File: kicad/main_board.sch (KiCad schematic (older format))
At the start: 55 parts, among them J1 Conn_01x07, J2 Conn_01x07, J3 Conn_01x07, J4 Conn_01x07, J5 Conn_01x07, J6 TYPE-C-31-M-12, J7 TYPE-C-31-M-12, Q1 Q_NPN_BEC, Q2 Q_NPN_BEC, Q3 Q_NPN_BEC, Q4 Q_NPN_BEC, Q5 Q_NPN_BEC, SW1 Reset, SW2 Boot, U1 esp32-s2-wroom, U2 XC6220B331MR, U3 USBLC6-2SC6, U4 USBLC6-2SC6, U5 LMV324, U6 LMV324

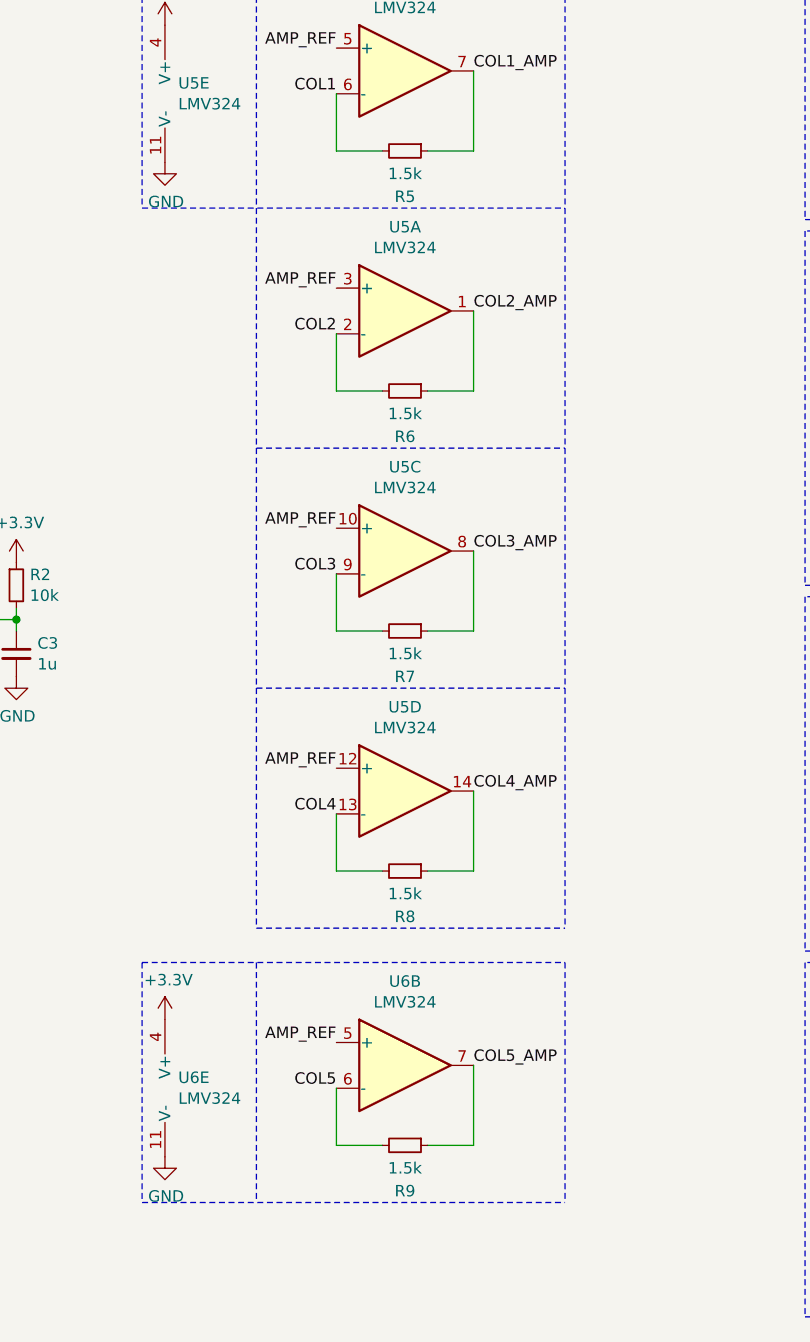
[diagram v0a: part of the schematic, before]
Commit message: Update the various sensitivity-related resistor values
This updates the transimpedance amplifier resistors to 2k, and adjusts
the LED drive resistors to an appropriate level, from empirical testing.
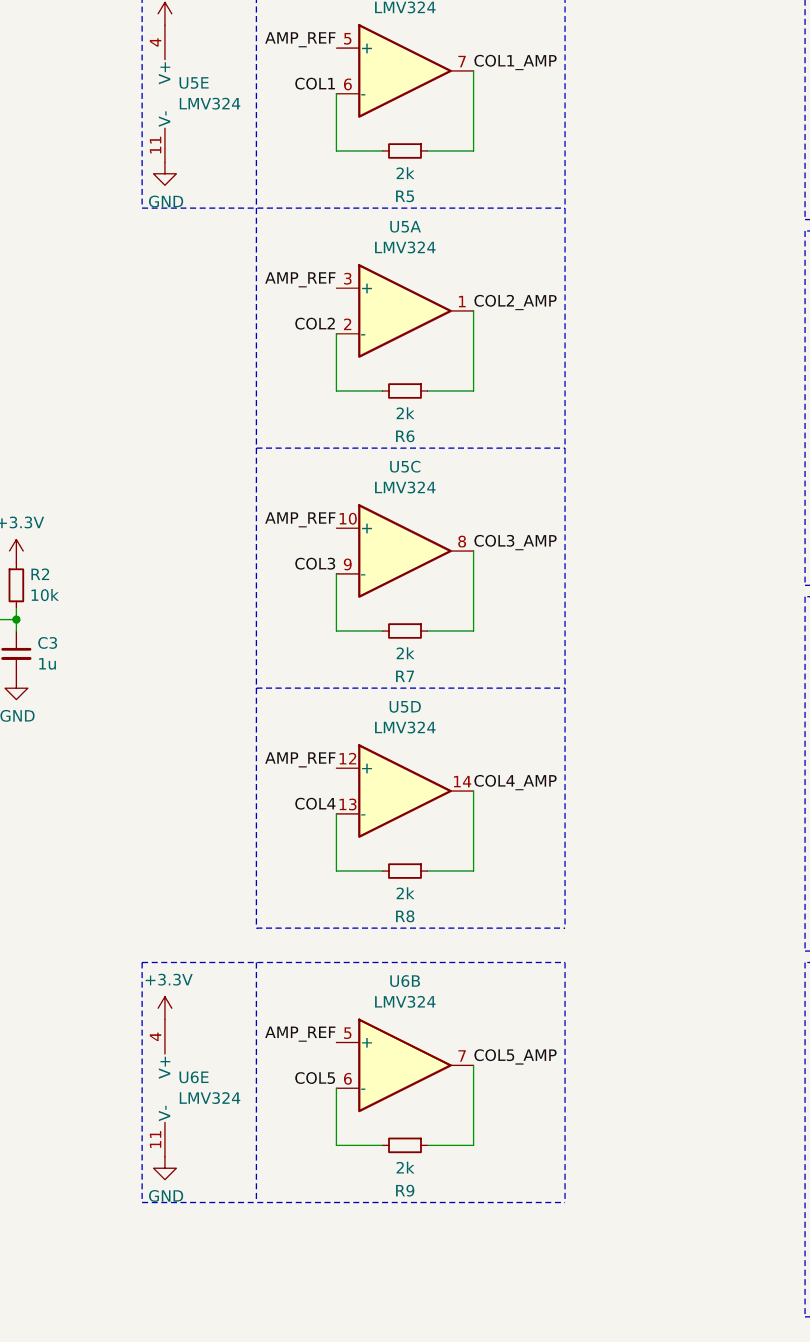
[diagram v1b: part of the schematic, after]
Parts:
- R5, R6, R7, R8, R9: value 1.5k -> 2k
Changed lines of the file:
@@
 P 6650 4650
 F 0 "R5" V 6850 4650 50  0000 C CNN
-F 1 "1.5k" V 6750 4650 50  0000 C CNN
+F 1 "2k" V 6750 4650 50  0000 C CNN
 F 2 "Resistor_SMD:R_0805_2012Metric_Pad1.15x1.40mm_HandSolder" H 6650 4650 50  0001 C CNN
 F 3 "~" H 6650 4650 50  0001 C CNN
@@
 P 6650 5700
 F 0 "R6" V 6850 5700 50  0000 C CNN
-F 1 "1.5k" V 6750 5700 50  0000 C CNN
+F 1 "2k" V 6750 5700 50  0000 C CNN
 F 2 "Resistor_SMD:R_0805_2012Metric_Pad1.15x1.40mm_HandSolder" H 6650 5700 50  0001 C CNN
 F 3 "~" H 6650 5700 50  0001 C CNN
@@
 P 6650 6750
 F 0 "R7" V 6850 6750 50  0000 C CNN
-F 1 "1.5k" V 6750 6750 50  0000 C CNN
+F 1 "2k" V 6750 6750 50  0000 C CNN
 F 2 "Resistor_SMD:R_0805_2012Metric_Pad1.15x1.40mm_HandSolder" H 6650 6750 50  0001 C CNN
 F 3 "~" H 6650 6750 50  0001 C CNN
@@
 P 6650 7800
 F 0 "R8" V 6850 7800 50  0000 C CNN
-F 1 "1.5k" V 6750 7800 50  0000 C CNN
+F 1 "2k" V 6750 7800 50  0000 C CNN
 F 2 "Resistor_SMD:R_0805_2012Metric_Pad1.15x1.40mm_HandSolder" H 6650 7800 50  0001 C CNN
 F 3 "~" H 6650 7800 50  0001 C CNN
@@
 P 6650 9000
 F 0 "R9" V 6850 9000 50  0000 C CNN
-F 1 "1.5k" V 6750 9000 50  0000 C CNN
+F 1 "2k" V 6750 9000 50  0000 C CNN
 F 2 "Resistor_SMD:R_0805_2012Metric_Pad1.15x1.40mm_HandSolder" H 6650 9000 50  0001 C CNN
 F 3 "~" H 6650 9000 50  0001 C CNN

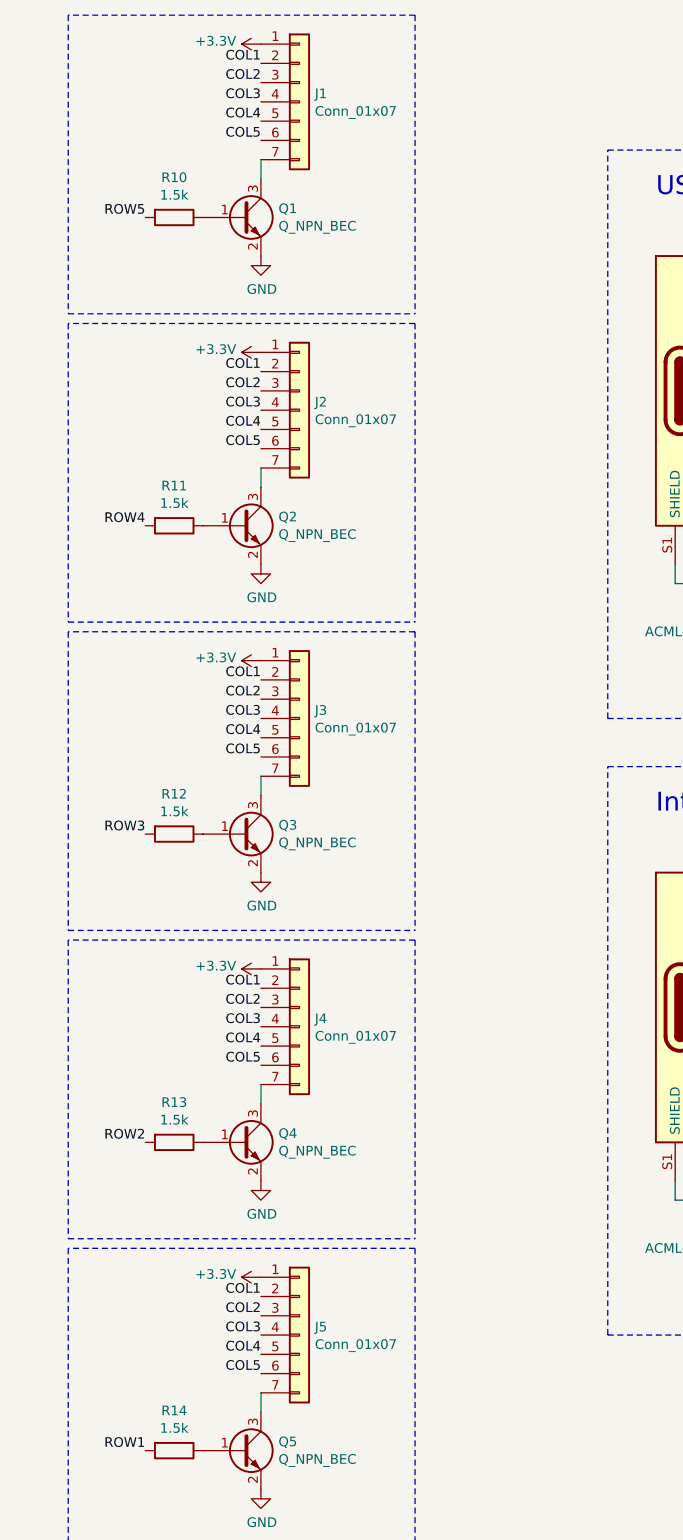
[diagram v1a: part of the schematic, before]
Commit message: Reverse the cluster connectors on the main board
This reverses the connectors, so the orientation is correct for a normally
wired cable.
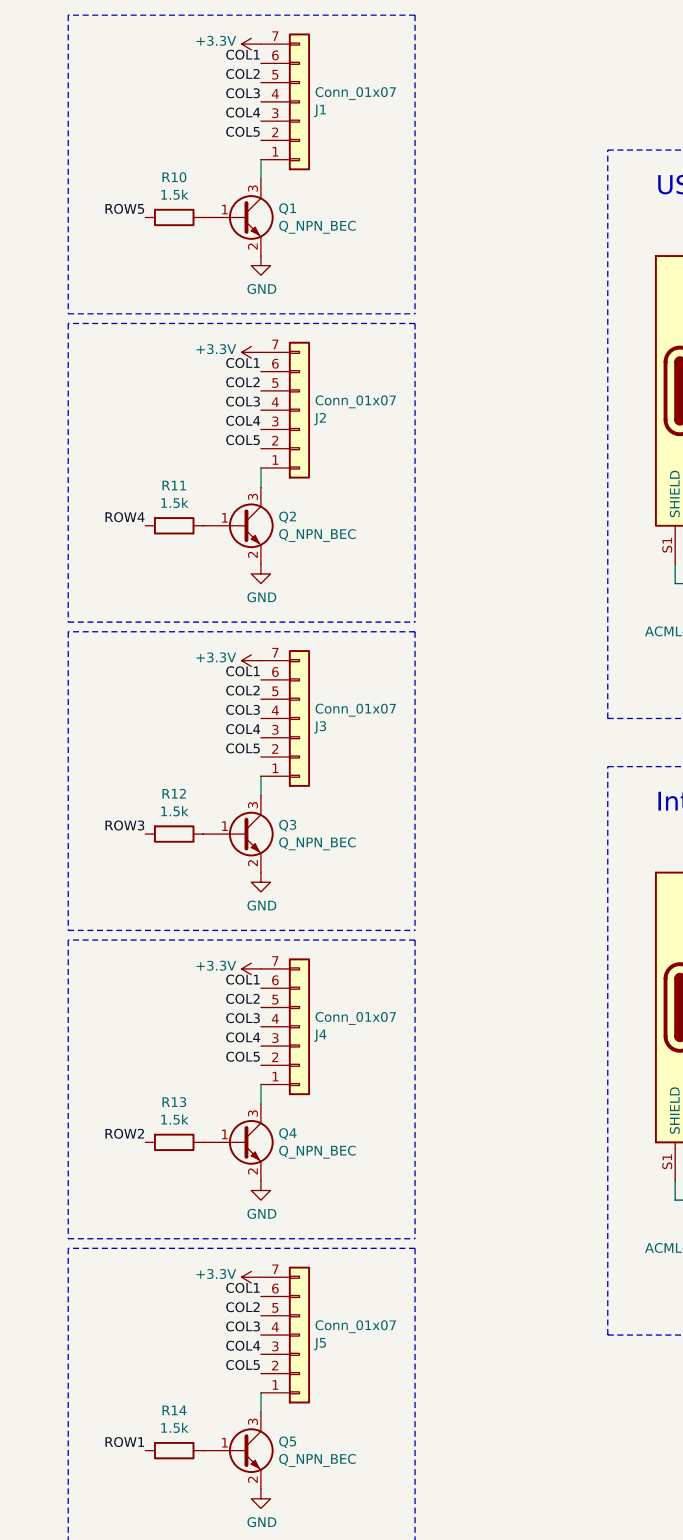
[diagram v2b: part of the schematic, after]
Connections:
- net +3V3: now also J1.7 (Pin_7), J2.7 (Pin_7), J3.7 (Pin_7), J4.7 (Pin_7), J5.7 (Pin_7); no longer J1.1 (Pin_1), J2.1 (Pin_1), J3.1 (Pin_1), J4.1 (Pin_1), J5.1 (Pin_1)
- net COL1: now also J1.6 (Pin_6), J2.6 (Pin_6), J3.6 (Pin_6), J4.6 (Pin_6), J5.6 (Pin_6); no longer J1.2 (Pin_2), J2.2 (Pin_2), J3.2 (Pin_2), J4.2 (Pin_2), J5.2 (Pin_2)
- net COL2: now also J1.5 (Pin_5), J2.5 (Pin_5), J3.5 (Pin_5), J4.5 (Pin_5), J5.5 (Pin_5); no longer J1.3 (Pin_3), J2.3 (Pin_3), J3.3 (Pin_3), J4.3 (Pin_3), J5.3 (Pin_3)
- net COL4: now also J1.3 (Pin_3), J2.3 (Pin_3), J3.3 (Pin_3), J4.3 (Pin_3), J5.3 (Pin_3); no longer J1.5 (Pin_5), J2.5 (Pin_5), J3.5 (Pin_5), J4.5 (Pin_5), J5.5 (Pin_5)
- net COL5: now also J1.2 (Pin_2), J2.2 (Pin_2), J3.2 (Pin_2), J4.2 (Pin_2), J5.2 (Pin_2); no longer J1.6 (Pin_6), J2.6 (Pin_6), J3.6 (Pin_6), J4.6 (Pin_6), J5.6 (Pin_6)
- net at Q1.3 (C): now also J1.1 (Pin_1); no longer J1.7 (Pin_7)
- net at Q2.3 (C): now also J2.1 (Pin_1); no longer J2.7 (Pin_7)
- net at Q3.3 (C): now also J3.1 (Pin_1); no longer J3.7 (Pin_7)
- net at Q4.3 (C): now also J4.1 (Pin_1); no longer J4.7 (Pin_7)
- net at Q5.3 (C): now also J5.1 (Pin_1); no longer J5.7 (Pin_7)
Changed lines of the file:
@@
-$EndComp
-$Comp
-L Connector_Generic:Conn_01x07 J1
-U 1 1 6072BBC9
-P 9600 2250
-F 0 "J1" H 9680 2292 50  0000 L CNN
-F 1 "Conn_01x07" H 9680 2201 50  0000 L CNN
-F 2 "lalboard:JST_ZH_B7B-ZR_1x07_P1.50mm_Vertical" H 9600 2250 50  0001 C CNN
-F 3 "~" H 9600 2250 50  0001 C CNN
-	1    9600 2250
-	1    0    0    -1
 $EndComp
 $Comp
@@
 $EndComp
 $Comp
-L Connector_Generic:Conn_01x07 J2
-U 1 1 6077F203
-P 9600 3850
-F 0 "J2" H 9680 3892 50  0000 L CNN
-F 1 "Conn_01x07" H 9680 3801 50  0000 L CNN
-F 2 "lalboard:JST_ZH_B7B-ZR_1x07_P1.50mm_Vertical" H 9600 3850 50  0001 C CNN
-F 3 "~" H 9600 3850 50  0001 C CNN
-	1    9600 3850
-	1    0    0    -1
-$EndComp
-$Comp
 L power:GND #PWR021
 U 1 1 6077F209
@@
 F 3 "~" H 9600 5450 50  0001 C CNN
 	1    9600 5450
-	1    0    0    -1
+	1    0    0    1
 $EndComp
 $Comp
@@
 F 3 "~" H 9600 7050 50  0001 C CNN
 	1    9600 7050
-	1    0    0    -1
+	1    0    0    1
 $EndComp
 $Comp
@@
 F 3 "~" H 9600 8650 50  0001 C CNN
 	1    9600 8650
-	1    0    0    -1
+	1    0    0    1
 $EndComp
 $Comp
@@
 Wire Notes Line
 	7350 8200 7350 9250
+$Comp
+L Connector_Generic:Conn_01x07 J1
+U 1 1 60C302B6
+P 9600 2250
+F 0 "J1" H 9680 2292 50  0000 L CNN
+F 1 "Conn_01x07" H 9680 2201 50  0000 L CNN
+F 2 "lalboard:JST_ZH_B7B-ZR_1x07_P1.50mm_Vertical" H 9600 2250 50  0001 C CNN
+F 3 "~" H 9600 2250 50  0001 C CNN
+	1    9600 2250
+	1    0    0    1
+$EndComp
+$Comp
+L Connector_Generic:Conn_01x07 J2
+U 1 1 6077F203
+P 9600 3850
+F 0 "J2" H 9680 3892 50  0000 L CNN
+F 1 "Conn_01x07" H 9680 3801 50  0000 L CNN
+F 2 "lalboard:JST_ZH_B7B-ZR_1x07_P1.50mm_Vertical" H 9600 3850 50  0001 C CNN
+F 3 "~" H 9600 3850 50  0001 C CNN
+	1    9600 3850
+	1    0    0    1
+$EndComp
 $EndSCHEMATC

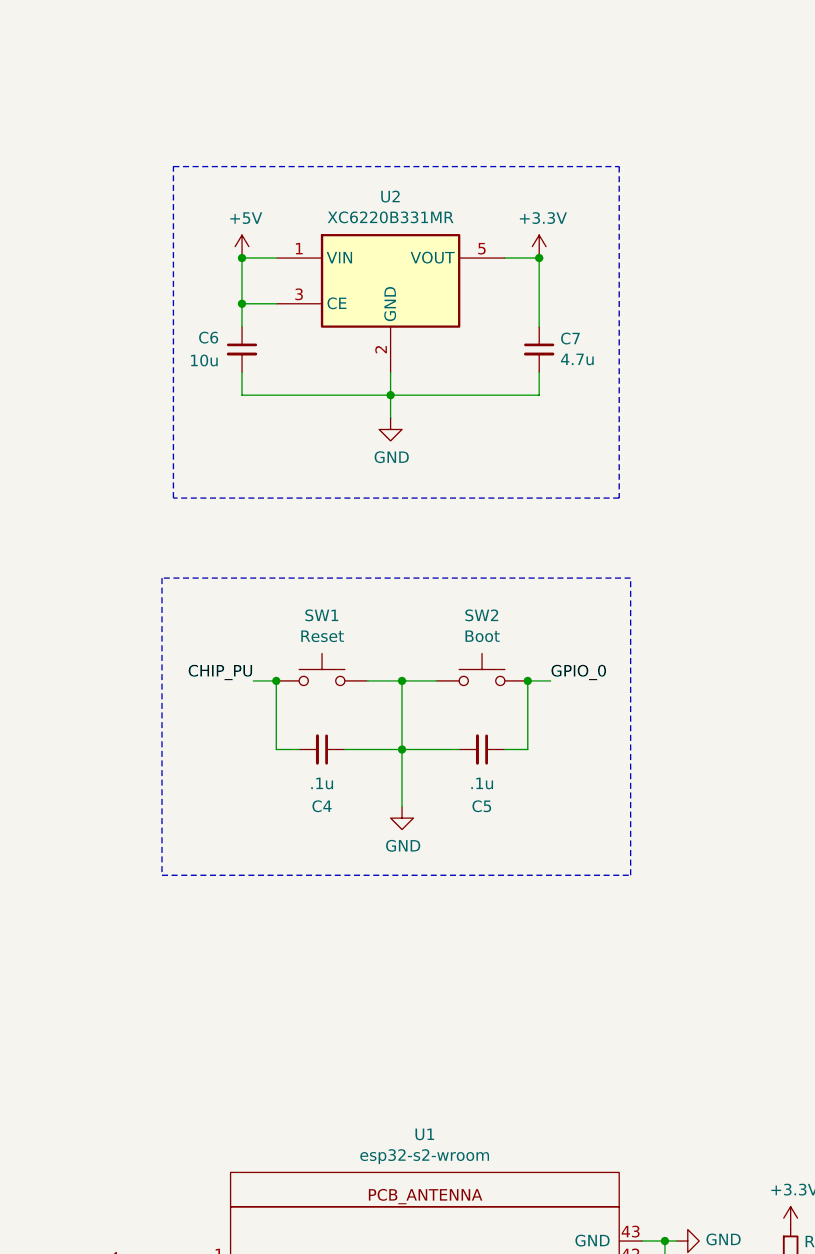
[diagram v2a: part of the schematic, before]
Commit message: Add a test connector to the main board
This adds an optional jst-zh connector that gives access to the output
signals from the opamps
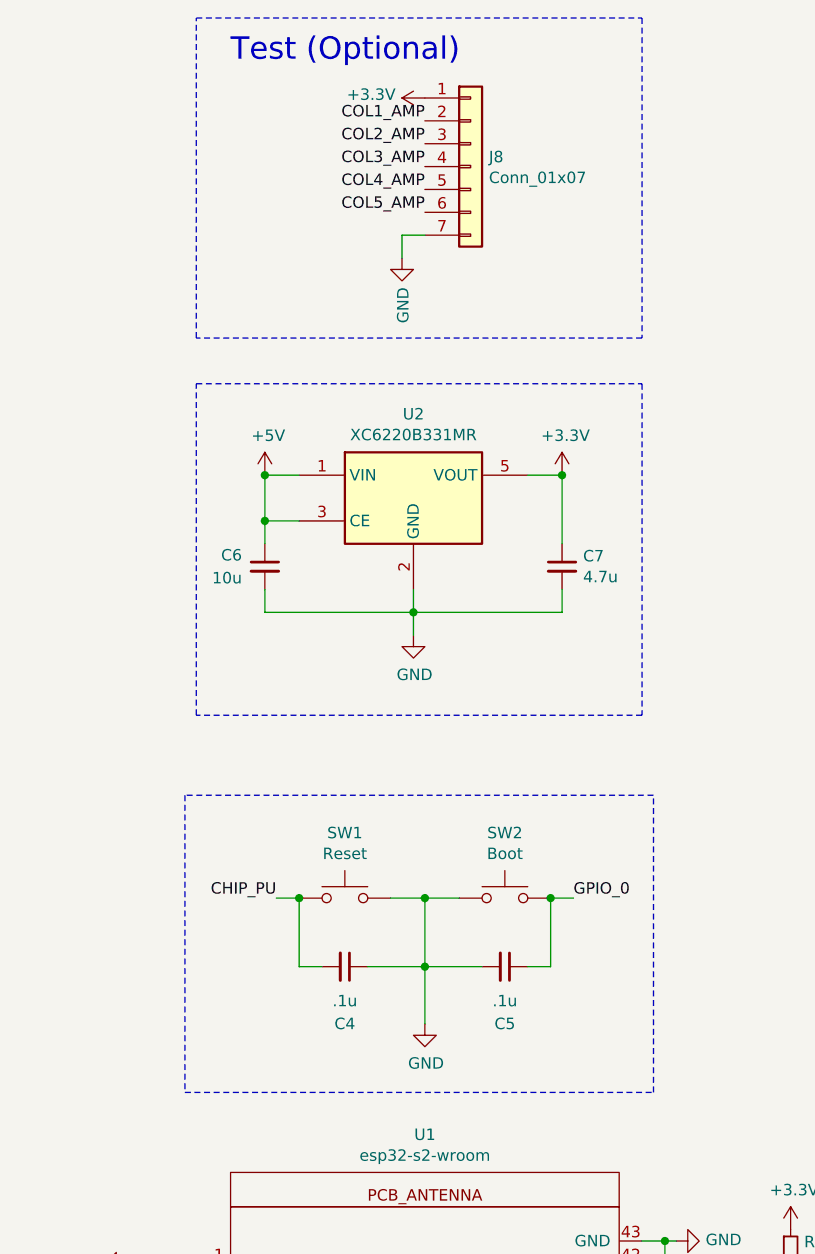
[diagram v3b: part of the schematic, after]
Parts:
- added J8: Conn_01x07, lalboard:JST_ZH_B7B-ZR_1x07_P1.50mm_Vertical, symbol Connector_Generic:Conn_01x07
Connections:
- net +3V3: now also J8.1 (Pin_1)
- net COL1_AMP: now also J8.2 (Pin_2)
- net COL2_AMP: now also J8.3 (Pin_3)
- net COL3_AMP: now also J8.4 (Pin_4)
- net COL4_AMP: now also J8.5 (Pin_5)
- net COL5_AMP: now also J8.6 (Pin_6)
- net GND: now also J8.7 (Pin_7)
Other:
- note added: "Test (Optional)"
- moved on the sheet: C4, C5, C6, C7, SW1, SW2, U2
